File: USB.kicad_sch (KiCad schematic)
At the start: 19 parts, among them J501 USB_A_Stacked, J502 USB_A_Stacked, U501 ASDMB-24.000MHz-C, U502 ASDMB-26.000MHz-C, U503 USB3343, U504 74LVC1G07, U505 USB2514B_Bi

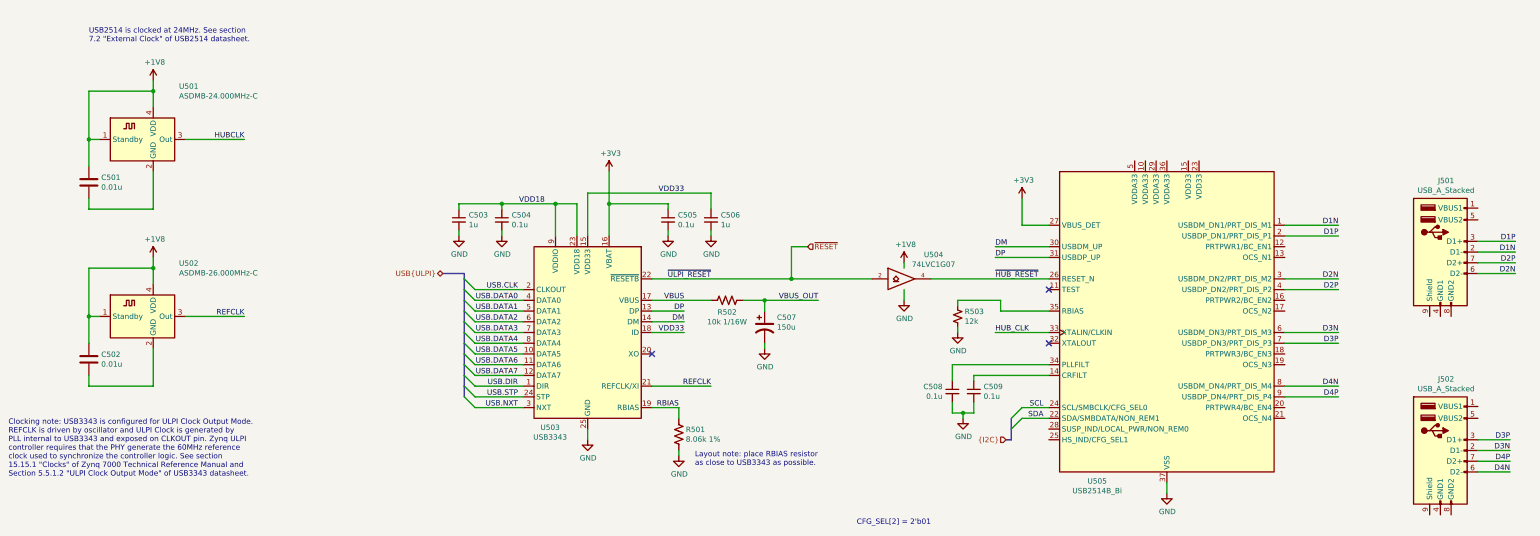
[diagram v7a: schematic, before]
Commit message: Connect USB clock generators to gnd, add clock termination resistor
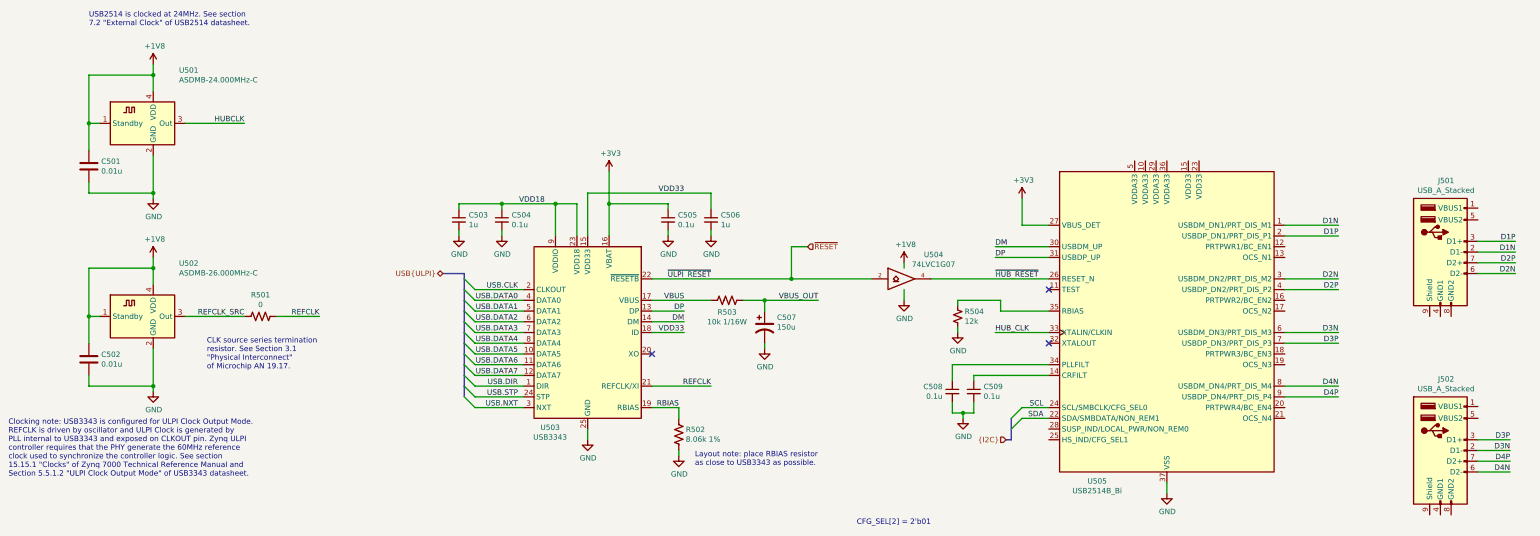
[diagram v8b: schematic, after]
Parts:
- added R501: 0, Resistor_SMD:R_0402_1005Metric, symbol Device:R_US
- renumbered R501 to R502, R502 to R503, R503 to R504
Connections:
- net GND: now also C501.2, C502.2, U501.2 (GND), U502.2 (GND)
- net REFCLK: now also R501.2; no longer U502.3 (Out)
- new net REFCLK_SRC: R501.1, U502.3 (Out)
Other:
- note added: "CLK source series termination resistor. See Section 3.1 "Physical Interconnect" of Microchip AN 19.17."
- moved on the sheet: C501, U501
